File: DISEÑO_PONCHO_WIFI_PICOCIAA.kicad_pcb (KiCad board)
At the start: 2 copper layers, 51 x 30.5 mm, 11 parts, among them P1 MOUNT_HOLE, P2 MOUNT_HOLE, U1 ESP-12E

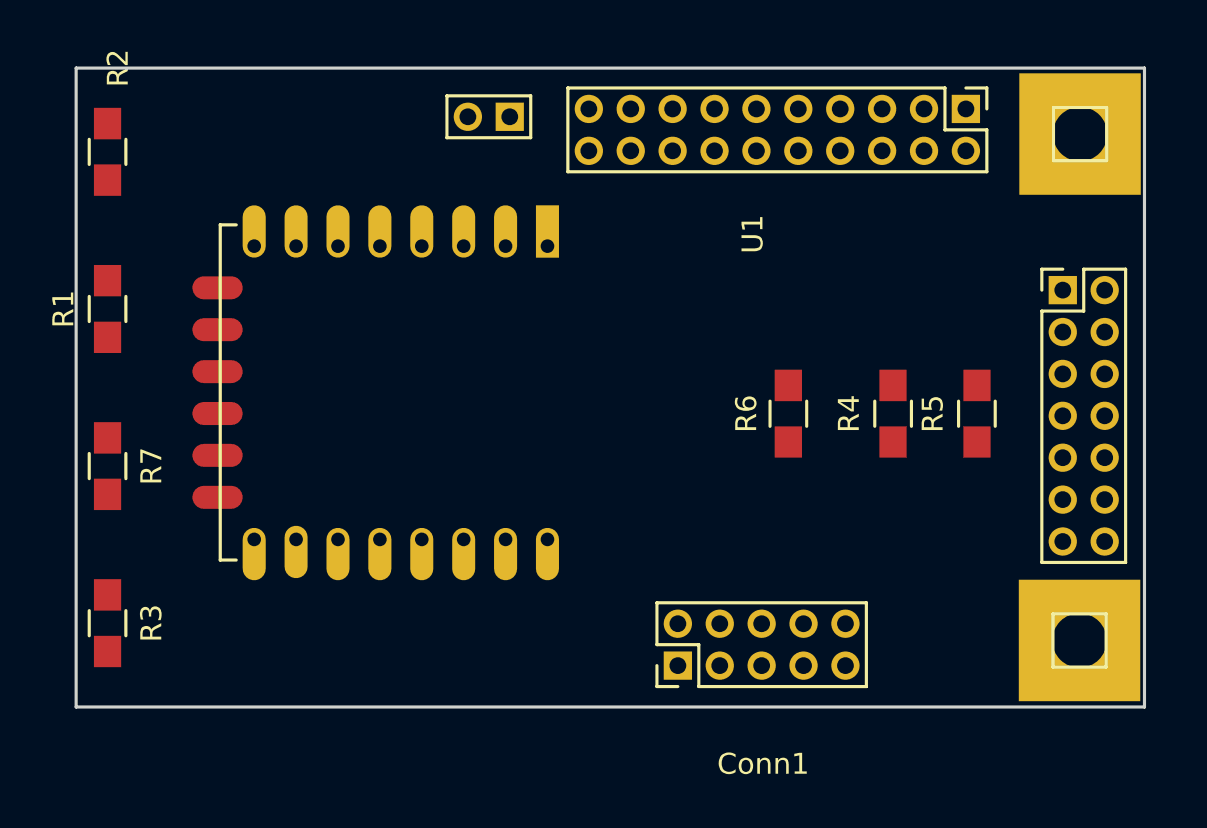
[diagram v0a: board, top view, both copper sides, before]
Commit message: Comentarios DB
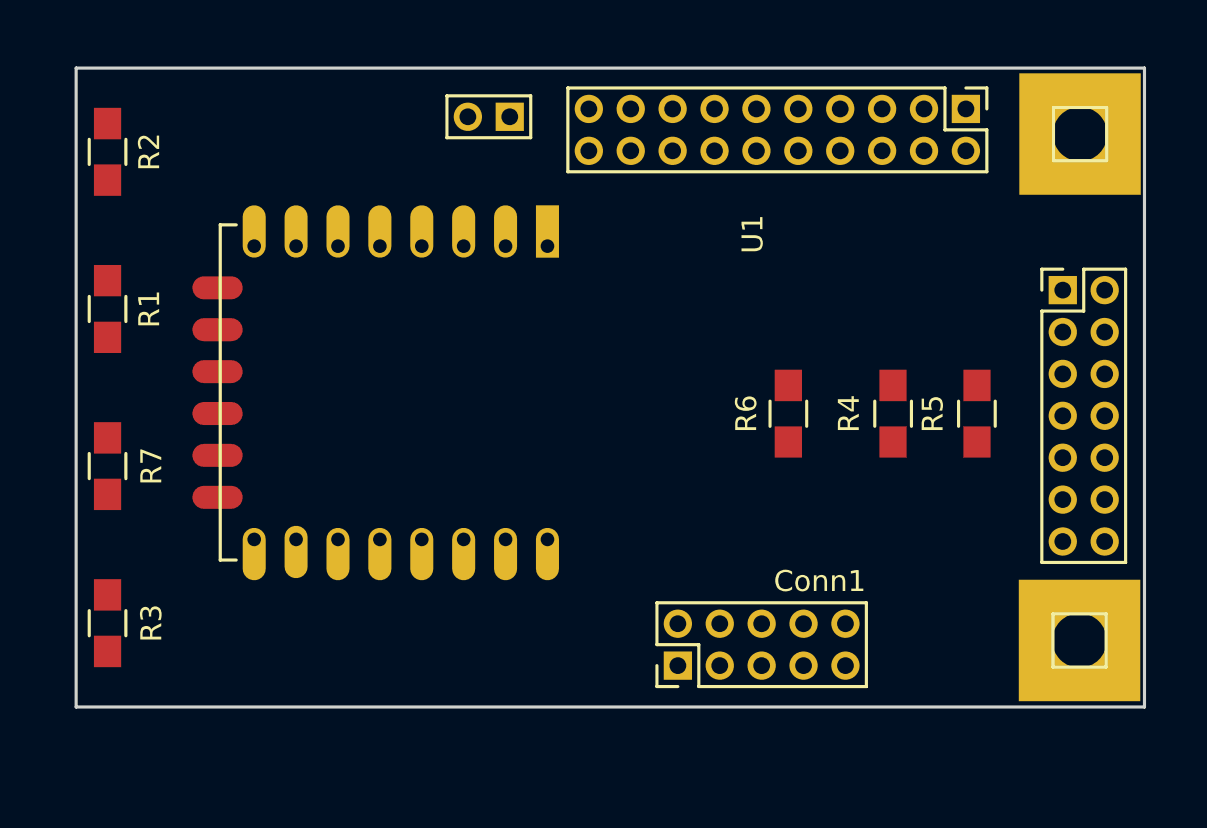
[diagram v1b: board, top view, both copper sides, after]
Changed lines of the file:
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@@
     (links 27)
     (no_connects 25)
-    (area 0 0 0 0)
+    (area 117.925 79.05 171.239858 118.3)
     (thickness 1.6)
     (drawings 4)
@@
   )
   (page A4)
+  (title_block
+    (title "Poncho Wifi PICO-CIAA")
+    (date 2016-12-19)
+    (rev 1.0)
+    (company FIUBA)
+    (comment 1 "Revisor: Sebastián López")
+    (comment 2 "Diseñado por: Sergio De Jesús")
+    (comment 3 "Licencias en LICENCIA_Y_COLABORADORES/LICENSE")
+  )
   (layers
     (0 F.Cu signal)
@@
   (module pico_ciaa_ponchos:Conn_Pico_Ciaa (layer F.Cu)
     (at 166.6 94.6)
-    (fp_text reference Conn1 (at -14.3 22.625) (layer F.SilkS)
+    (fp_text reference Conn1 (at -11.6 13.9) (layer F.SilkS)
       (effects (font (size 1 1) (thickness 0.15)))
     )
@@
     (tags "resistor 0805")
     (attr smd)
-    (fp_text reference R1 (at 0 -2.1 90) (layer F.SilkS)
+    (fp_text reference R1 (at 0 2 90) (layer F.SilkS)
       (effects (font (size 1 1) (thickness 0.15)))
     )
@@
     (tags "resistor 0805")
     (attr smd)
-    (fp_text reference R2 (at -4 -0.5 270) (layer F.SilkS)
-      (effects (font (size 1 1) (thickness 0.15)))
-    )
+    (fp_text reference R2 (at 0 -2 270) (layer F.SilkS)
+      (effects (font (size 1 1) (thickness 0.15)))
+    )

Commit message: Ruteo y limpieza de proyecto
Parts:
- added FID1: FIDUCIAL, Poncho_wifi:Fiducial_1mm_Dia_2.54mm_Outer_CopperTop, F.Cu at (162.5, 91.5)
- added FID2: FIDUCIAL, Poncho_wifi:Fiducial_1mm_Dia_2.54mm_Outer_CopperTop, F.Cu at (161.0, 110.0)
- added FID3: FIDUCIAL, Poncho_wifi:Fiducial_1mm_Dia_2.54mm_Outer_CopperTop, F.Cu at (126.5, 86.5)
- added G101: Logo_OSHWA, Poncho_wifi:Logo_OSHWA, F.Cu at (157.0, 93.5)
- moved R1 0.50 mm to (121.5, 95.5)
- moved R2 0.50 mm to (121.5, 88.0)
- moved R3 0.50 mm to (121.5, 110.5)
- moved R7 0.50 mm to (121.5, 103.0)
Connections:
- net +3V3 renamed +3.3V
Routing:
- net +3.3V: track 0.00 -> 87.7 mm
- net Net-(Conn1-Pad14): track 0.00 -> 65.9 mm, vias 0 -> 1
- net Net-(Conn1-Pad39): track 0.00 -> 42.2 mm
- net Net-(Conn1-Pad44): track 0.00 -> 39.5 mm, vias 0 -> 2
- net Net-(Conn1-Pad41): track 0.00 -> 38.7 mm, vias 0 -> 1
- net Net-(R2-Pad1): track 0.00 -> 23.6 mm, vias 0 -> 2
- net Net-(R1-Pad1): track 0.00 -> 22.8 mm, vias 0 -> 2
- net Net-(Conn1-Pad37): track 0.00 -> 12.5 mm
- net Net-(R3-Pad2): track 0.00 -> 12.5 mm
- net Net-(R7-Pad2): track 0.00 -> 12.4 mm, vias 0 -> 2
- net Net-(Conn1-Pad40): track 0.00 -> 10.4 mm
- net GND: track 0.00 -> 9.95 mm, vias 0 -> 1
- added copper zone on B.Cu, net GND
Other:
- net class Default: clearance 0.2 -> 0.3; trace_width 0.25 -> 0.3; via_dia 0.6 -> 1.27; via_drill 0.4 -> 0.7
- rule trace_clearance: 0.2 -> 0.3
- rule trace_min: 0.2 -> 0.3
- rule via_min_drill: 0.3 -> 0.7
- rule via_min_size: 0.4 -> 1.27
- board text added: "Capas de cobre: 2"
- board text added: "Espesor de placa: 1.4mm Espesor de cobre: 1Oz Soporte FR4"
- board text added: "Estándar de fabricación: Mayer 12 mils Según documento encontrado en: CONSIDERACIONES_INICIALES/FABRICANTES\ DE\ PCB/estandares.pdf"
- board text added: "Industria Argentina"
- board text added: "Poncho wifi PicoCIAA"
- board text added: "Sergio De Jesús"
- board text added: "StackUp"
- board text added: "v1.0"

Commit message: Se introducen comentarios de SL
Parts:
- removed R4, R5: R, Resistors_SMD:R_0805_HandSoldering
- added G***: LOGO, Poncho_wifi:Logo_Poncho, F.Cu at (160.5, 103.5)
- U1: footprint pico_ciaa_ponchos:ESP-12E -> ESP-12E
- moved R6 2.24 mm to (155.5, 99.5)
- moved U1 2.00 mm to (144.0, 92.5)
- moved G101 0.71 mm to (157.5, 93.0)
- moved R1 0.50 mm to (122.0, 95.5)
- moved R2 0.50 mm to (122.0, 88.0)
- moved R3 0.50 mm to (122.0, 110.5)
- moved R7 0.50 mm to (122.0, 103.0)
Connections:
- net +3.3V renamed +3V3
- R1 pad 1: Net-(R1-Pad1) -> Net-(Conn1-Pad11)
- U1 pad 1: Net-(R1-Pad1) -> Net-(Conn1-Pad11)
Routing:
- net Net-(Conn1-Pad11): track 0.00 -> 51.4 mm
- net GND: track 9.95 -> 36.9 mm, vias 1 -> 0
- net Net-(R1-Pad1): track 22.8 -> 0.00 mm, vias 2 -> 0
- net Net-(Conn1-Pad41): track 38.7 -> 17.7 mm, vias 1 -> 0
- net Net-(Conn1-Pad44): track 39.5 -> 21.6 mm, vias 2 -> 0
- net Net-(Conn1-Pad14): track 65.9 -> 57.6 mm, vias 1 -> 0
- net +3V3: track 87.7 -> 80.6 mm
- net Net-(Conn1-Pad37): track 12.5 -> 9.89 mm
- net Net-(R2-Pad1): track 23.6 -> 26.2 mm, vias 2 -> 0
- net Net-(Conn1-Pad40): track 10.4 -> 7.89 mm
- net Net-(R3-Pad2): track 12.5 -> 14.3 mm
- net Net-(R7-Pad2): track 12.4 -> 13.5 mm, vias 2 -> 0
